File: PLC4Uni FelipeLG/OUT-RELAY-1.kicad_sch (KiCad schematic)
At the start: 7 parts, among them K1 Fujitsu_FTR-LYCA005x, Q10 BFN26

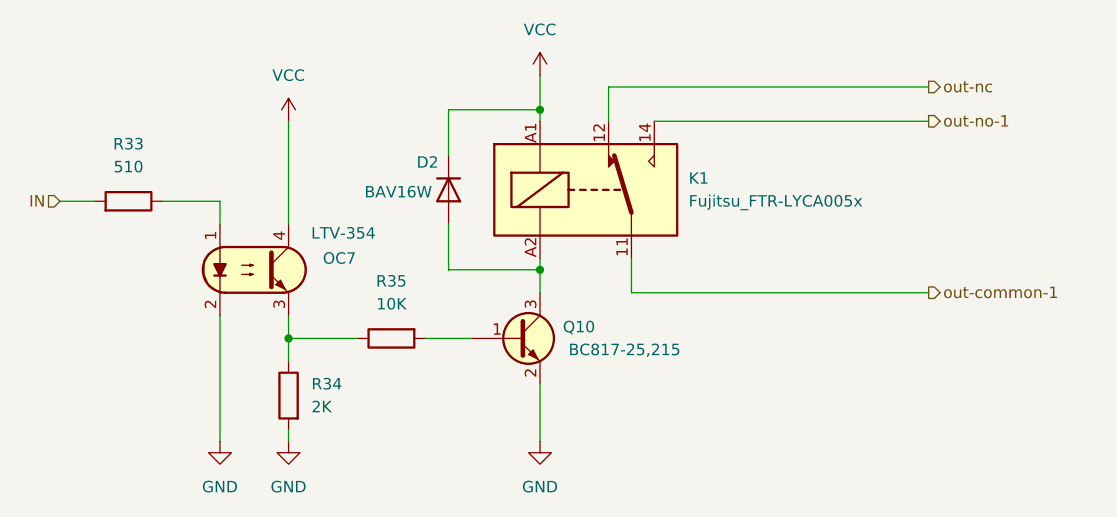
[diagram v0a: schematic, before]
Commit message: Add files via upload
Updated Circuitos corregidos y pistas agregadas
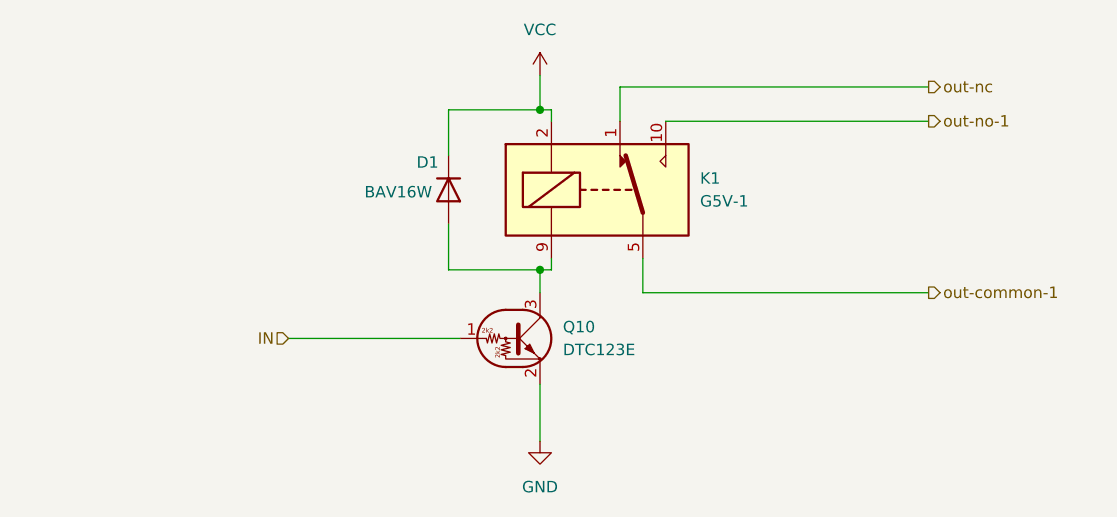
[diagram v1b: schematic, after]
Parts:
- removed K1: Fujitsu_FTR-LYCA005x, Relay_THT:Relay_SPDT_Fujitsu_FTR-LYCA005x_FormC_Vertical, symbol Relay:Fujitsu_FTR-LYCA005x
- removed OC7: FOD817S, Package_DIP_AKL:SMDIP-4_W9.53mm, symbol Optocoupler_AKL:FOD817S
- removed Q10: BFN26, Package_TO_SOT_SMD_AKL:SOT-23, symbol Transistor_BJT_AKL:BFN26
- removed R33: 510, Resistor_SMD_AKL:R_0603_1608Metric, symbol Resistor_AKL:R_0603
- removed R34: 2K, Resistor_SMD_AKL:R_0603_1608Metric, symbol Resistor_AKL:R_0603
- removed R35: 10K, Resistor_SMD_AKL:R_0603_1608Metric, symbol Resistor_AKL:R_0603
- added K1: G5V-1, Relay_THT:Relay_SPDT_Omron_G5V-1, symbol Relay:G5V-1
- added Q10: DTC123E, Package_TO_SOT_SMD:SOT-23, symbol Transistor_BJT:DTC123E
- renumbered D2 to D1
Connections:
- net GND: now also Q10.2 (E)
- net IN: now also Q10.1 (B)
- net VCC: now also K1.2
- net out-common-1: now also K1.5, K1.6
- net out-nc: now also K1.1
- net out-no-1: now also K1.10
- net at D1.2 (A): now also K1.9, Q10.3 (C)
